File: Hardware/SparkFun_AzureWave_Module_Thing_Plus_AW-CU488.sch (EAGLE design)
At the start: 60 parts, among them J1 THING_PLUS, J3 QWIIC_RA, J5 USB-C, Q1 3.1A/30V/105mΩ, Q2 MBT3904DW1T1, U2 CP210X, U3 AP2112K-3.3V, U4 MCP73831

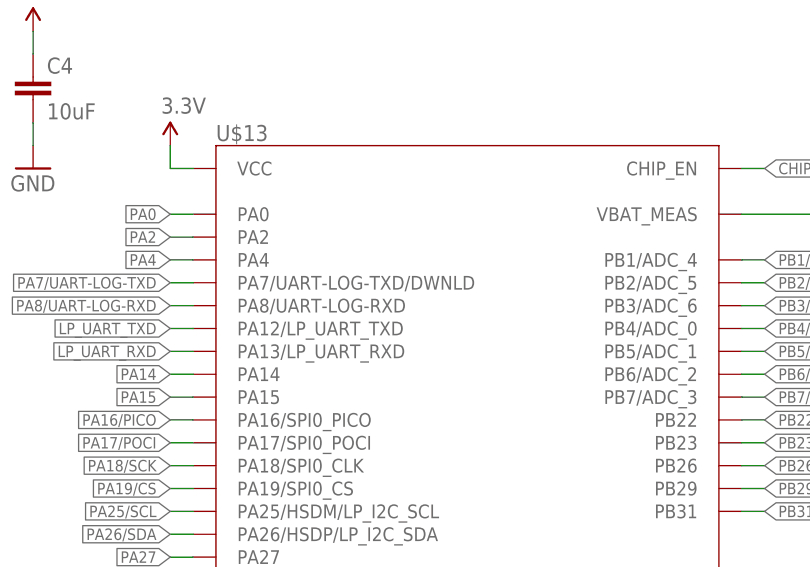
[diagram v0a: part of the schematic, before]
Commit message: made symbol pin name for download active low
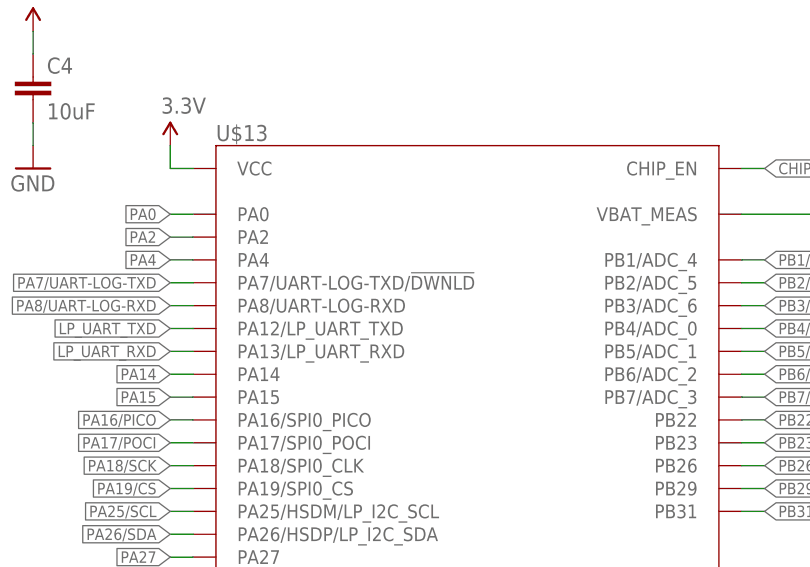
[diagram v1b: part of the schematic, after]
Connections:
- net PA7/UART-LOG-TXD: now also U$13.PA7/UART-LOG-TXD/!DWNLD!; no longer U$13.PA7/UART-LOG-TXD/DWNLD
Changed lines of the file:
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@@
 <wire x1="63.5" y1="114.3" x2="60.96" y2="114.3" width="0.1524" layer="91"/>
 <label x="60.96" y="114.3" size="1.27" layer="95" font="vector" rot="R180" xref="yes"/>
-<pinref part="U$13" gate="G$1" pin="PA7/UART-LOG-TXD/DWNLD"/>
+<pinref part="U$13" gate="G$1" pin="PA7/UART-LOG-TXD/!DWNLD!"/>
 </segment>
 <segment>

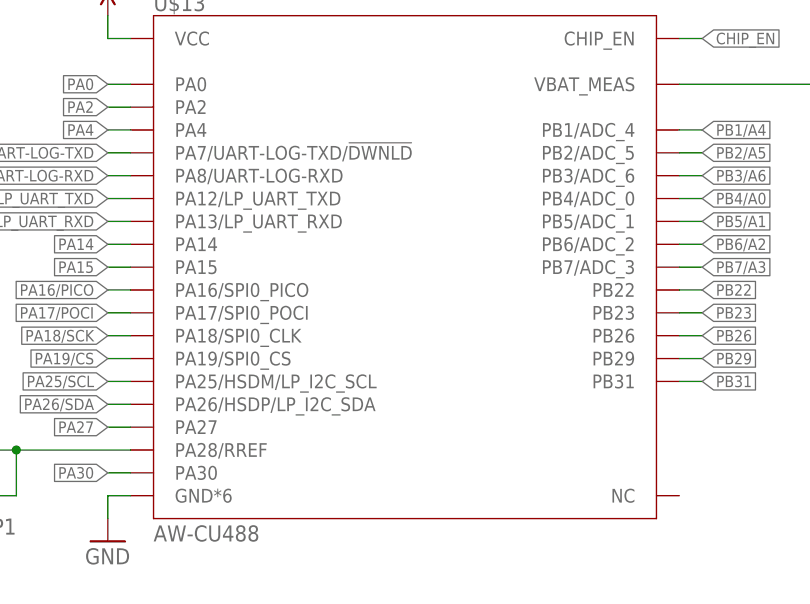
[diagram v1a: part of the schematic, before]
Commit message: final check finds
-Scooted VIN trace for GND flow near Vreg
-nudged trace off of PA27 to avoid acid trap
-updated pin names to include SWD functions in symbol
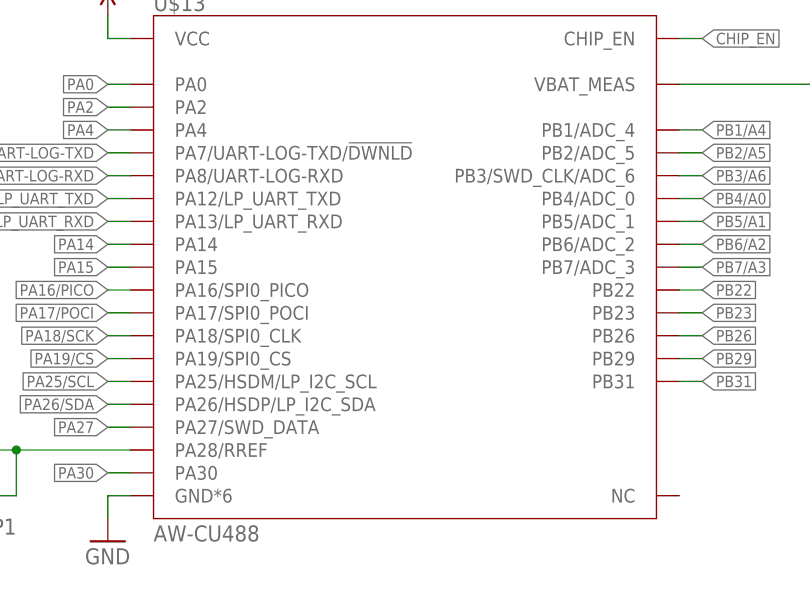
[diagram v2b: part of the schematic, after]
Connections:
- net PA27: now also U$13.PA27/SWD_DATA; no longer U$13.PA27
- net PB3/A6: now also U$13.PB3/SWD_CLK/ADC_6; no longer U$13.PB3/ADC_6
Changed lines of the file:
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@@
 <wire x1="63.5" y1="83.82" x2="60.96" y2="83.82" width="0.1524" layer="91"/>
 <label x="60.96" y="83.82" size="1.27" layer="95" font="vector" rot="R180" xref="yes"/>
-<pinref part="U$13" gate="G$1" pin="PA27"/>
+<pinref part="U$13" gate="G$1" pin="PA27/SWD_DATA"/>
 </segment>
 <segment>
@@
 <net name="PB3/A6" class="0">
 <segment>
-<pinref part="U$13" gate="G$1" pin="PB3/ADC_6"/>
+<pinref part="U$13" gate="G$1" pin="PB3/SWD_CLK/ADC_6"/>
 <wire x1="124.46" y1="111.76" x2="127" y2="111.76" width="0.1524" layer="91"/>
 <label x="127" y="111.76" size="1.27" layer="95" font="vector" xref="yes"/>

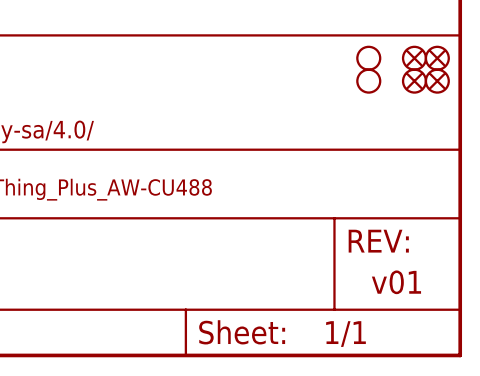
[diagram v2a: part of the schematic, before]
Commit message: Re-routed traces off of charge current select jumper
-The traces were unnecessarily tight off the jumpers and easy to cut on accident. Now they have more clearance.
-Also bumped version to v10 in brd and sch
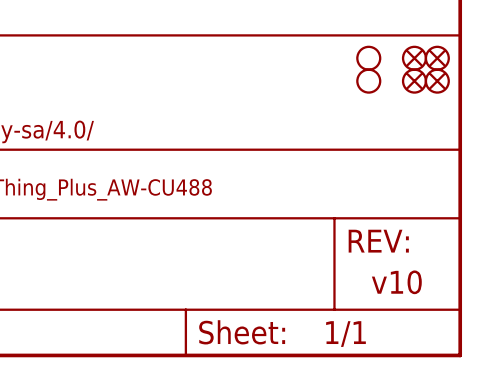
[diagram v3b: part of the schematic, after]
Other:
- note added: "v10"
- note removed: "v01"
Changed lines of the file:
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@@
 <text x="91.44" y="175.26" size="2.54" layer="94" font="vector" align="bottom-center">AzureWave AW-CU488 Module</text>
 <text x="363.22" y="175.26" size="2.54" layer="94" font="vector" align="bottom-center">Thing Plus Headers</text>
-<text x="421.894" y="9.398" size="2.54" layer="94" font="vector" align="top-left">v01</text>
+<text x="421.894" y="9.398" size="2.54" layer="94" font="vector" align="top-left">v10</text>
 <text x="381" y="99.06" size="2.54" layer="94" font="vector" align="bottom-center">QWIIC Connector</text>
 <text x="353.314" y="11.43" size="2.54" layer="94" font="vector">Pete Lewis</text>

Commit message: changes found during proto testing
-removed R14 pulldown on reset button. It now pulls down directly to GND when pressed.
-adjusted Charge LED resistor to lower brightness (R3 changed from 1K to 4.7K)
-Added PTH header breakouts for UART LOG RX and TX.
-Changed silk on all pins to more user-friendly/common digital numbers.
-Added jumpers to more easily remove auto-boot circuit if needed for advanced use cases
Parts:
- removed J2, J4: (no value), SparkFun-Connectors:CONN_031X03_NO_SILK
- removed R14: 10k, SparkFun-Resistors:10KOHM-0402T-1/16W-1%
- removed TP1: TEST-POINTTP_15TH_THRU, SparkFun-Connectors:TEST-POINTTP_15TH_THRU
- added J6, J7: (no value), SparkFun-Connectors:CONN_05NO_SILK
- added JP1, JP3: JUMPER-SMT_2_NC_TRACE_SILK, SparkFun-Jumpers:JUMPER-SMT_2_NC_TRACE_SILK
- R3: value 1k -> 4.7k; device SparkFun-Resistors:1KOHM-0402T-1/16W-1% -> SparkFun-Resistors:4.7KOHM-0402T-1/16W-1%
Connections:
- new net N$6: JP1.1, Q2G1.C
- net CHIP_EN: now also JP1.2; no longer Q2G1.C
- net GND: now also J7.1, S1.3, S1.4; no longer R14.2
- net N$10: now also JP3.1, Q2G2.C; no longer R14.1, S1.3, S1.4
- net PA0: now also J6.1; no longer J2.1
- net PA14: now also J7.2; no longer J4.1
- net PA15: now also J7.3; no longer J4.2
- net PA2: now also J6.3; no longer J2.3
- net PA27: now also J7.4; no longer J4.3
- net PA28: now also J7.5; no longer TP1.1
- net PA4: now also J6.2; no longer J2.2
- net PA7/UART-LOG-TXD: now also J6.4, JP3.2; no longer Q2G2.C
- net PA8/UART-LOG-RXD: now also J6.5
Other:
- note added: "Cut JP1 and JP3 to disable auto-boot circuit"
- moved on the sheet: Q2G1, Q2G2, R17, R18

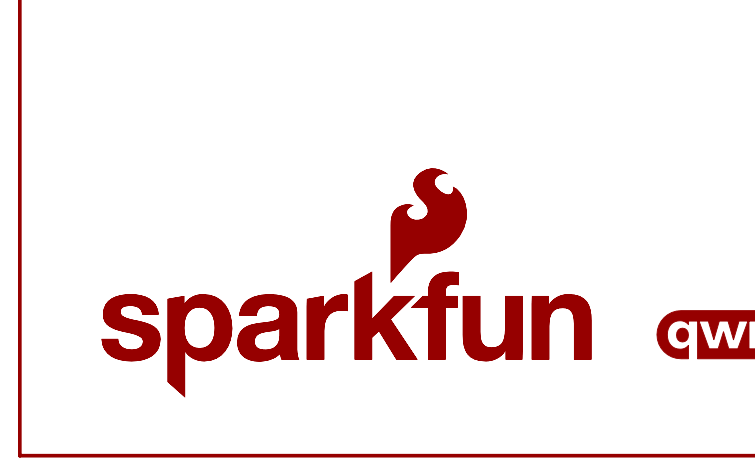
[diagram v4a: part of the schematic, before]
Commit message: centered SFE logo and product name text
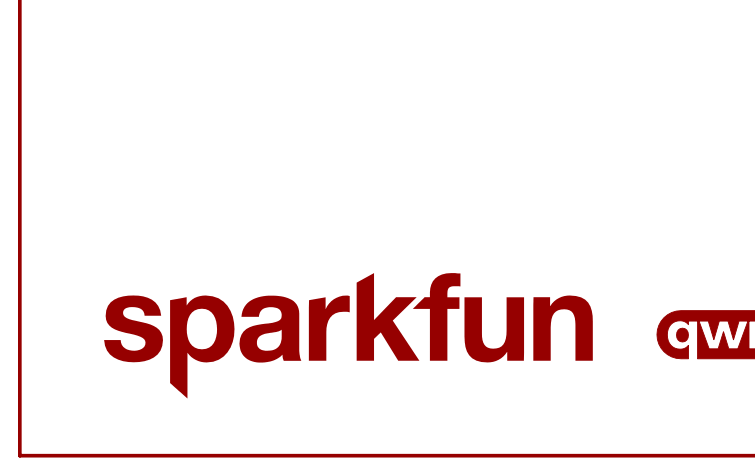
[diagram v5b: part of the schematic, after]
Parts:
- removed LOGO3, LOGO5: SFE_LOGO_NAME_FLAME.1_INCH, SparkFun-Aesthetics:SFE_LOGO_NAME_FLAME.1_INCH
- added LOGO1: SFE_LOGO_NAME.1_INCH, SparkFun-Aesthetics:SFE_LOGO_NAME.1_INCH
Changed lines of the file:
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@@
 <part name="GND5" library="SparkFun-PowerSymbols" deviceset="GND" device=""/>
 <part name="R8" library="SparkFun-Resistors" deviceset="100KOHM" device="-0402T-1/16W-1%" value="100k"/>
-<part name="LOGO3" library="SparkFun-Aesthetics" deviceset="SFE_LOGO_NAME_FLAME" device=".1_INCH"/>
 <part name="LOGO4" library="SparkFun-Aesthetics" deviceset="FOUR_LAYER_WARNING" device=""/>
 <part name="FD1" library="SparkFun-Aesthetics" deviceset="FIDUCIAL" device="UFIDUCIAL"/>
@@
 <part name="R18" library="SparkFun-Resistors" deviceset="10KOHM" device="-0402T-1/16W-1%" value="10k"/>
 <part name="Q2" library="SparkFun-DiscreteSemi" deviceset="TRANS_NPN_DUAL" device="-MBT3904DW1T1" value="MBT3904DW1T1"/>
-<part name="LOGO5" library="SparkFun-Aesthetics" deviceset="SFE_LOGO_NAME_FLAME" device=".1_INCH"/>
 <part name="SUPPLY12" library="SparkFun-PowerSymbols" deviceset="V_USB" device=""/>
 <part name="SUPPLY15" library="SparkFun-PowerSymbols" deviceset="V_BATT" device=""/>
@@
 <part name="JP1" library="SparkFun-Jumpers" deviceset="JUMPER-SMT_2_NC_TRACE" device="_SILK" package3d_urn="urn:adsk.eagle:package:39281/1" value=""/>
 <part name="JP3" library="SparkFun-Jumpers" deviceset="JUMPER-SMT_2_NC_TRACE" device="_SILK" package3d_urn="urn:adsk.eagle:package:39281/1" value=""/>
+<part name="LOGO1" library="SparkFun-Aesthetics" deviceset="SFE_LOGO_NAME" device=".1_INCH"/>
 </parts>
 <sheets>
@@
 <attribute name="VALUE" x="60.96" y="219.456" size="1.778" layer="96" font="vector" align="top-center"/>
 </instance>
-<instance part="LOGO3" gate="G$1" x="8.382" y="6.096" smashed="yes"/>
 <instance part="LOGO4" gate="G$1" x="331.978" y="37.592" smashed="yes"/>
 <instance part="FD1" gate="G$1" x="429.26" y="33.02" smashed="yes"/>
@@
 <attribute name="VALUE" x="231.648" y="120.904" size="1.778" layer="96" font="vector" rot="MR180"/>
 </instance>
-<instance part="LOGO5" gate="G$1" x="8.382" y="6.096" smashed="yes"/>
 <instance part="SUPPLY12" gate="G$1" x="12.7" y="236.22" smashed="yes">
 <attribute name="VALUE" x="12.7" y="239.014" size="1.778" layer="96" font="vector" align="bottom-center"/>
@@
 <attribute name="VALUE" x="238.76" y="111.252" size="1.778" layer="96" font="vector" align="center"/>
 </instance>
+<instance part="LOGO1" gate="G$1" x="7.366" y="6.35" smashed="yes"/>
 </instances>
 <busses>

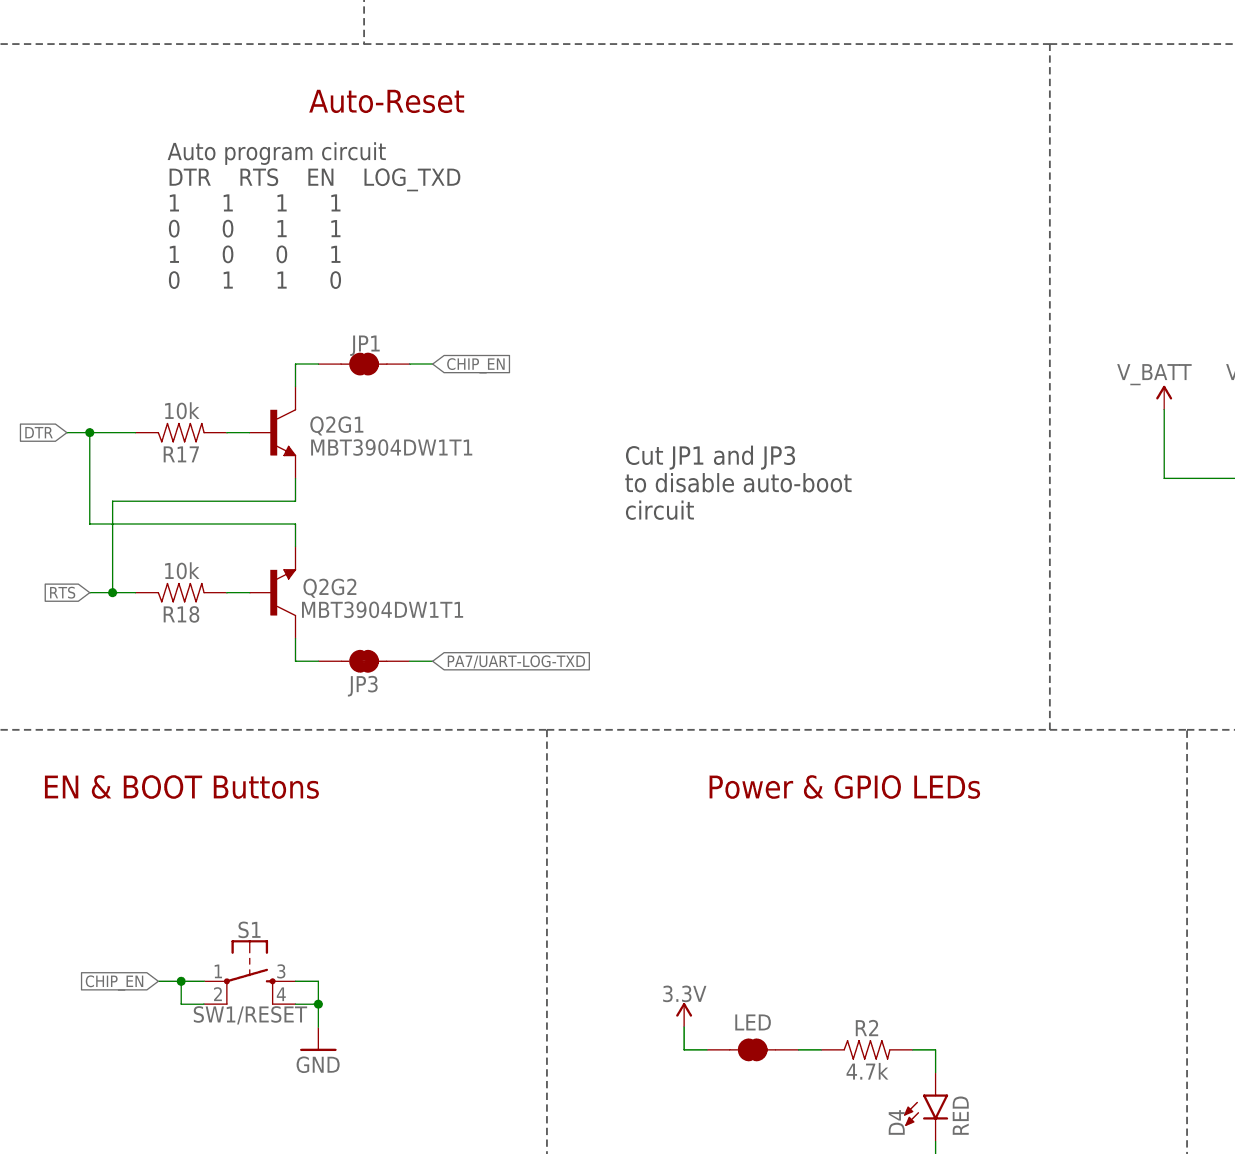
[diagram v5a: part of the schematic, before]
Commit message: Reds review catches
-added note in SCH about pwr LED jumper
-approved jumper overlap DRC errors
-added table lines to schematic info about auto-reset
-moved OSHW logo over via
-removed unncessary GND vias under USB-C
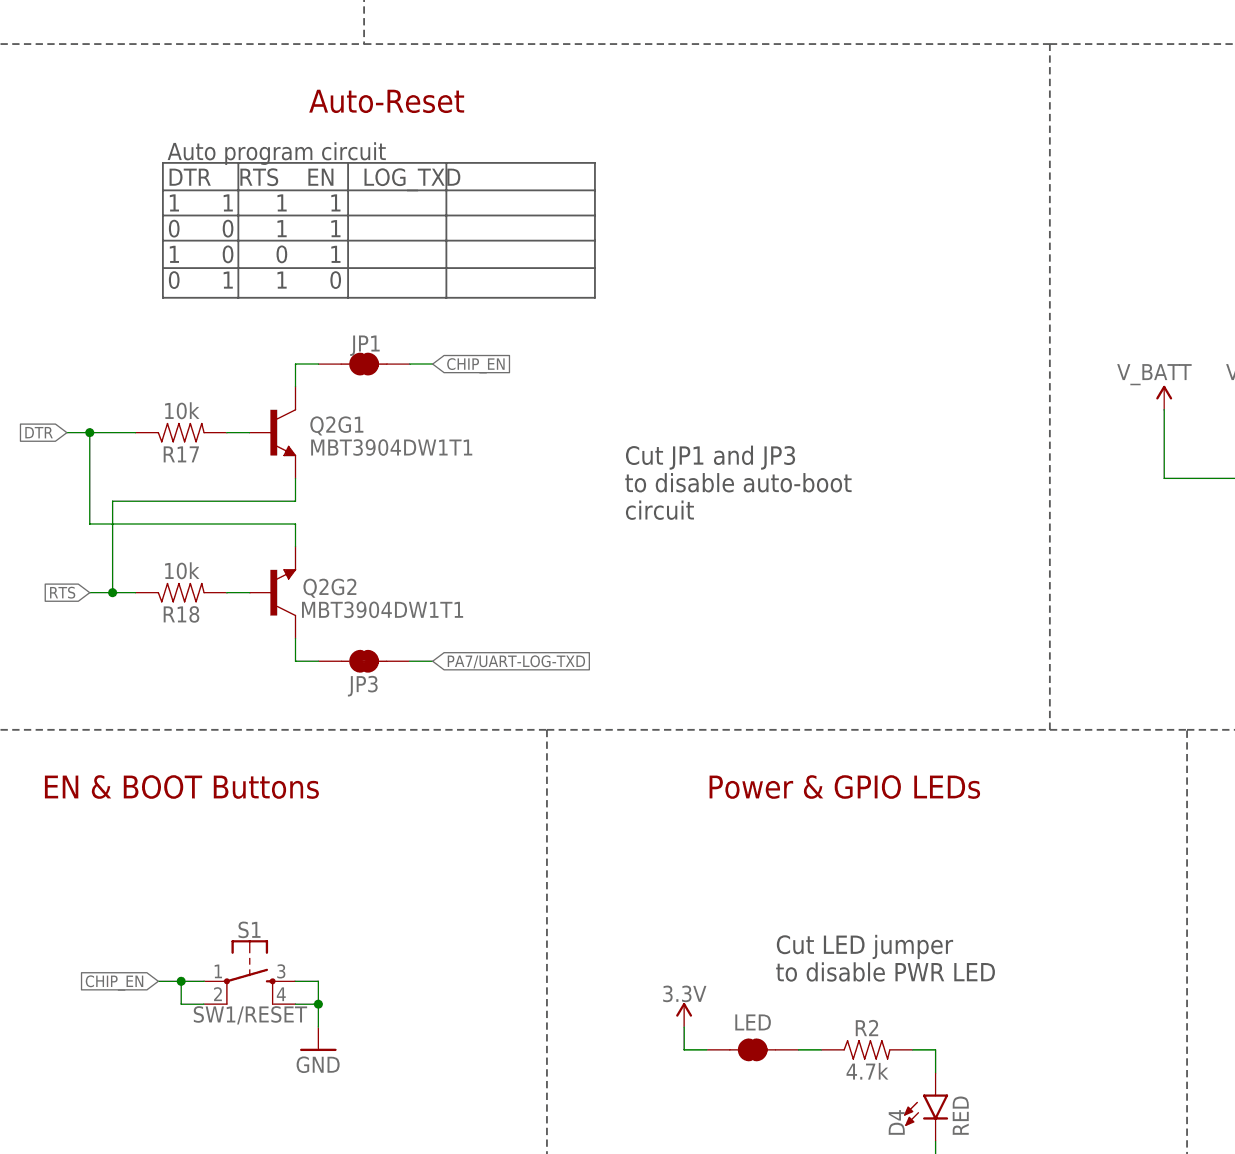
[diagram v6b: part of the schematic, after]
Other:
- note added: "Cut LED jumper to disable PWR LED"
